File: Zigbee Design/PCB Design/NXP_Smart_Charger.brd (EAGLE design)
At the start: 108.3 x 63.3 mm, 83 parts, among them IC1 MID400, IC2 MID400, IC3 LMV358, IC4 LMV358, Q1 2222A, Q2 2222A

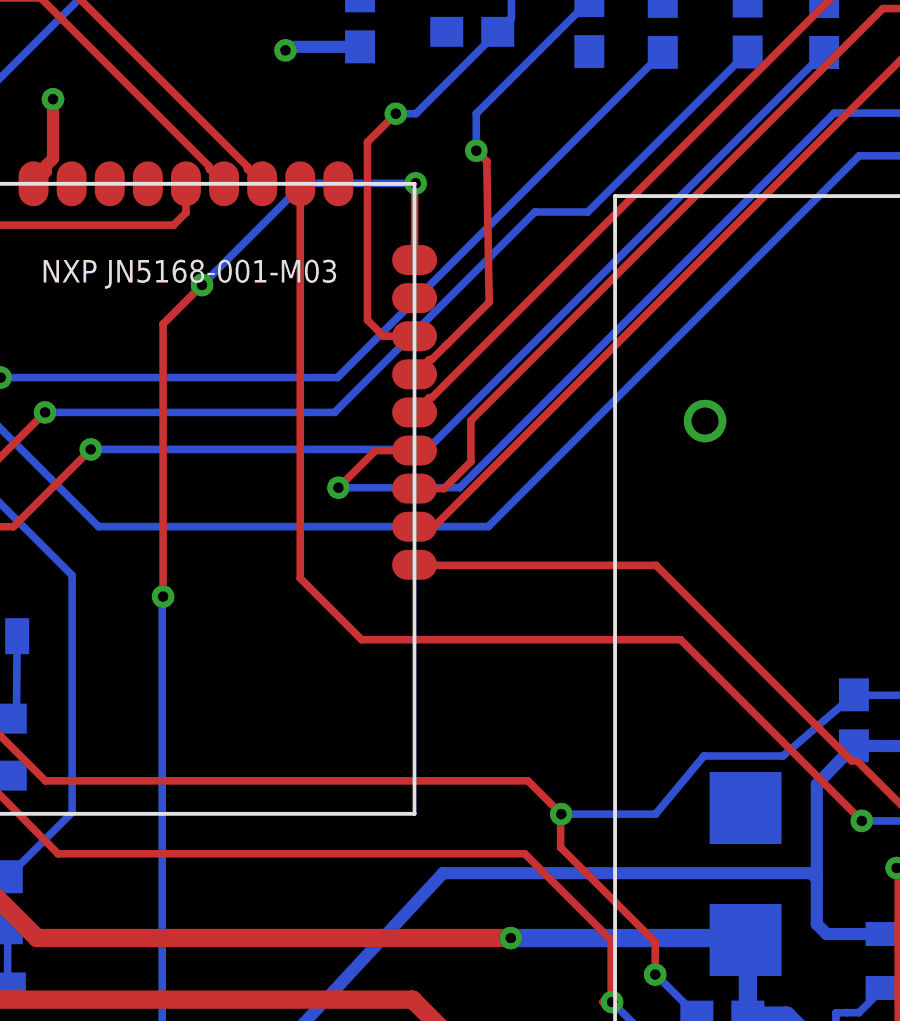
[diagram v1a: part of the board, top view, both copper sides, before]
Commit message: added flash memory
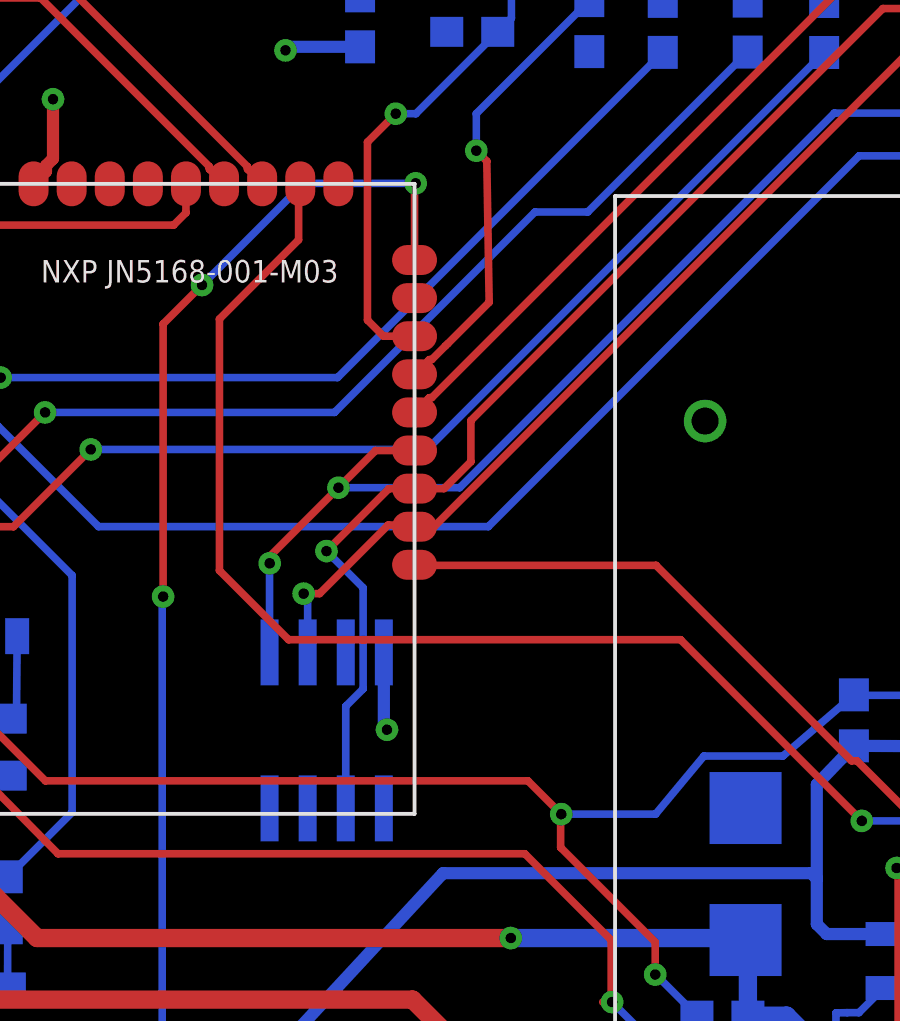
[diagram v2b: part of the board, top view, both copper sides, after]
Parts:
- added U1: M25P40, Smart_Charger:SO-08
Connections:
- new net HOLD: U1.7
- new net SS1: U1.1
- new net WP: U1.3
- net 3.3V: now also U1.8
- net GND: now also U1.4
- net MISO: now also U1.2
- net MOSI: now also U1.5
- net SPI_CLK: now also U1.6
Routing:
- net MISO: track 49.5 -> 62.7 mm, vias 0 -> 1
- net SPI_CLK: track 51.8 -> 58.5 mm, vias 0 -> 1
- net MOSI: track 59.4 -> 65.8 mm, vias 1 -> 2
- net PWM: track 45.6 -> 49.3 mm
- net 3.3V: track 32.0 -> 34.6 mm, vias 2 -> 3
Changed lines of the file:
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@@
 <attribute name="PROD_ID" value="CONN-08438" x="29.944059375" y="61.788040625" size="1.778" layer="27" display="off"/>
 </element>
+<element name="U1" library="Smart_Charger" package="SO-08" value="M25P40" x="31.407103125" y="33.853121875" rot="MR0"/>
 </elements>
 <signals>
@@
 <via x="49.24298125" y="30.8356" extent="1-16" drill="0.35"/>
 <wire x1="49.24298125" y1="30.8356" x2="43.2028625" y2="36.87571875" width="0.254" layer="1"/>
-<wire x1="43.2028625" y1="36.87571875" x2="32.572959375" y2="36.87571875" width="0.254" layer="1"/>
-<wire x1="32.572959375" y1="36.87571875" x2="30.52571875" y2="38.922959375" width="0.254" layer="1"/>
-<wire x1="30.52571875" y1="38.922959375" x2="30.52571875" y2="52.07254375" width="0.254" layer="1"/>
+<wire x1="43.2028625" y1="36.87571875" x2="32.654240625" y2="36.87571875" width="0.254" layer="1"/>
+<wire x1="32.654240625" y1="36.87571875" x2="32.572959375" y2="36.87571875" width="0.254" layer="1"/>
 <wire x1="54.188359375" y1="29.606240625" x2="52.959" y2="30.8356" width="0.254" layer="16"/>
+<wire x1="32.654240625" y1="36.87571875" x2="30.137103125" y2="36.87571875" width="0.254" layer="1"/>
+<wire x1="30.137103125" y1="36.87571875" x2="27.83078125" y2="39.182040625" width="0.254" layer="1"/>
+<wire x1="27.83078125" y1="39.182040625" x2="27.83078125" y2="47.564040625" width="0.254" layer="1"/>
+<wire x1="27.83078125" y1="47.564040625" x2="30.469840625" y2="50.2031" width="0.254" layer="1"/>
+<wire x1="30.469840625" y1="50.2031" x2="30.469840625" y2="52.016665625" width="0.254" layer="1"/>
+<wire x1="30.469840625" y1="52.016665625" x2="30.52571875" y2="52.07254375" width="0.254" layer="1"/>
 </signal>
 <signal name="N$2">
@@
 <wire x1="36.21278125" y1="44.1807625" x2="36.21278125" y2="42.809159375" width="0.254" layer="1"/>
 <wire x1="36.21278125" y1="42.809159375" x2="35.316165625" y2="41.91254375" width="0.254" layer="1"/>
-<wire x1="35.316165625" y1="41.91254375" x2="34.33571875" y2="41.91254375" width="0.254" layer="1"/>
+<wire x1="34.33571875" y1="41.91254375" x2="35.316165625" y2="41.91254375" width="0.254" layer="1"/>
+<contactref element="U1" pad="2"/>
+<wire x1="32.042103125" y1="31.253121875" x2="32.042103125" y2="34.657996875" width="0.254" layer="16"/>
+<wire x1="32.042103125" y1="34.657996875" x2="32.6215" y2="35.23739375" width="0.254" layer="16"/>
+<wire x1="32.6215" y1="35.23739375" x2="32.6215" y2="38.607721875" width="0.254" layer="16"/>
+<wire x1="32.6215" y1="38.607721875" x2="31.39948125" y2="39.829740625" width="0.254" layer="16"/>
+<via x="31.39948125" y="39.829740625" extent="1-16" drill="0.35"/>
+<wire x1="31.39948125" y1="39.829740625" x2="33.482284375" y2="41.91254375" width="0.254" layer="1"/>
+<wire x1="33.482284375" y1="41.91254375" x2="34.33571875" y2="41.91254375" width="0.254" layer="1"/>
 </signal>
 <signal name="MOSI">
@@
 <wire x1="31.798259375" y1="41.94301875" x2="33.037784375" y2="43.18254375" width="0.254" layer="1"/>
 <wire x1="33.037784375" y1="43.18254375" x2="34.33571875" y2="43.18254375" width="0.254" layer="1"/>
+<contactref element="U1" pad="5"/>
+<wire x1="29.502103125" y1="36.453121875" x2="29.502103125" y2="39.4182625" width="0.254" layer="16"/>
+<wire x1="29.502103125" y1="39.4182625" x2="29.50718125" y2="39.423340625" width="0.254" layer="16"/>
+<via x="29.50718125" y="39.423340625" extent="1-16" drill="0.35"/>
+<wire x1="29.50718125" y1="39.423340625" x2="29.50718125" y2="39.651940625" width="0.254" layer="1"/>
+<wire x1="29.50718125" y1="39.651940625" x2="31.798259375" y2="41.94301875" width="0.254" layer="1"/>
 </signal>
 <signal name="GND">
@@
 <wire x1="22.28341875" y1="52.91024375" x2="22.28341875" y2="54.891940625" width="0.4064" layer="1"/>
 <via x="22.28341875" y="54.891940625" extent="1-16" drill="0.35"/>
+<contactref element="U1" pad="4"/>
 </signal>
 <signal name="BUTTON3">
@@
 <wire x1="30.15175625" y1="56.638878125" x2="30.032959375" y2="56.52008125" width="0.4064" layer="16"/>
 <via x="30.032959375" y="56.52008125" extent="1-16" drill="0.35" shape="square"/>
+<contactref element="U1" pad="8"/>
+<wire x1="33.312103125" y1="36.453121875" x2="33.312103125" y2="33.98011875" width="0.4064" layer="16"/>
+<wire x1="33.312103125" y1="33.98011875" x2="33.416240625" y2="33.87598125" width="0.4064" layer="16"/>
+<via x="33.416240625" y="33.87598125" extent="1-16" drill="0.35"/>
 </signal>
 <signal name="N$5">
@@
 <wire x1="75.4334" y1="56.45911875" x2="50.8" y2="56.45911875" width="0.254" layer="1"/>
 <wire x1="50.8" y1="56.45911875" x2="34.983425" y2="40.64254375" width="0.254" layer="1"/>
-<wire x1="34.983425" y1="40.64254375" x2="34.33571875" y2="40.64254375" width="0.254" layer="1"/>
+<wire x1="34.33571875" y1="40.64254375" x2="34.983425" y2="40.64254375" width="0.254" layer="1"/>
+<contactref element="U1" pad="6"/>
+<wire x1="30.772103125" y1="36.453121875" x2="30.772103125" y2="38.277796875" width="0.254" layer="16"/>
+<wire x1="30.772103125" y1="38.277796875" x2="30.63748125" y2="38.41241875" width="0.254" layer="16"/>
+<via x="30.63748125" y="38.41241875" extent="1-16" drill="0.35"/>
+<wire x1="30.63748125" y1="38.41241875" x2="31.17088125" y2="38.41241875" width="0.254" layer="1"/>
+<wire x1="31.17088125" y1="38.41241875" x2="33.45688125" y2="40.69841875" width="0.254" layer="1"/>
+<wire x1="33.45688125" y1="40.69841875" x2="34.27984375" y2="40.69841875" width="0.254" layer="1"/>
+<wire x1="34.27984375" y1="40.69841875" x2="34.33571875" y2="40.64254375" width="0.254" layer="1"/>
 </signal>
 <signal name="L6">
@@
 <wire x1="33.3019375" y1="46.99254375" x2="34.33571875" y2="46.99254375" width="0.254" layer="1"/>
 </signal>
+<signal name="HOLD">
+<contactref element="U1" pad="7"/>
+</signal>
+<signal name="SS1">
+<contactref element="U1" pad="1"/>
+</signal>
+<signal name="WP">
+<contactref element="U1" pad="3"/>
+</signal>
 </signals>

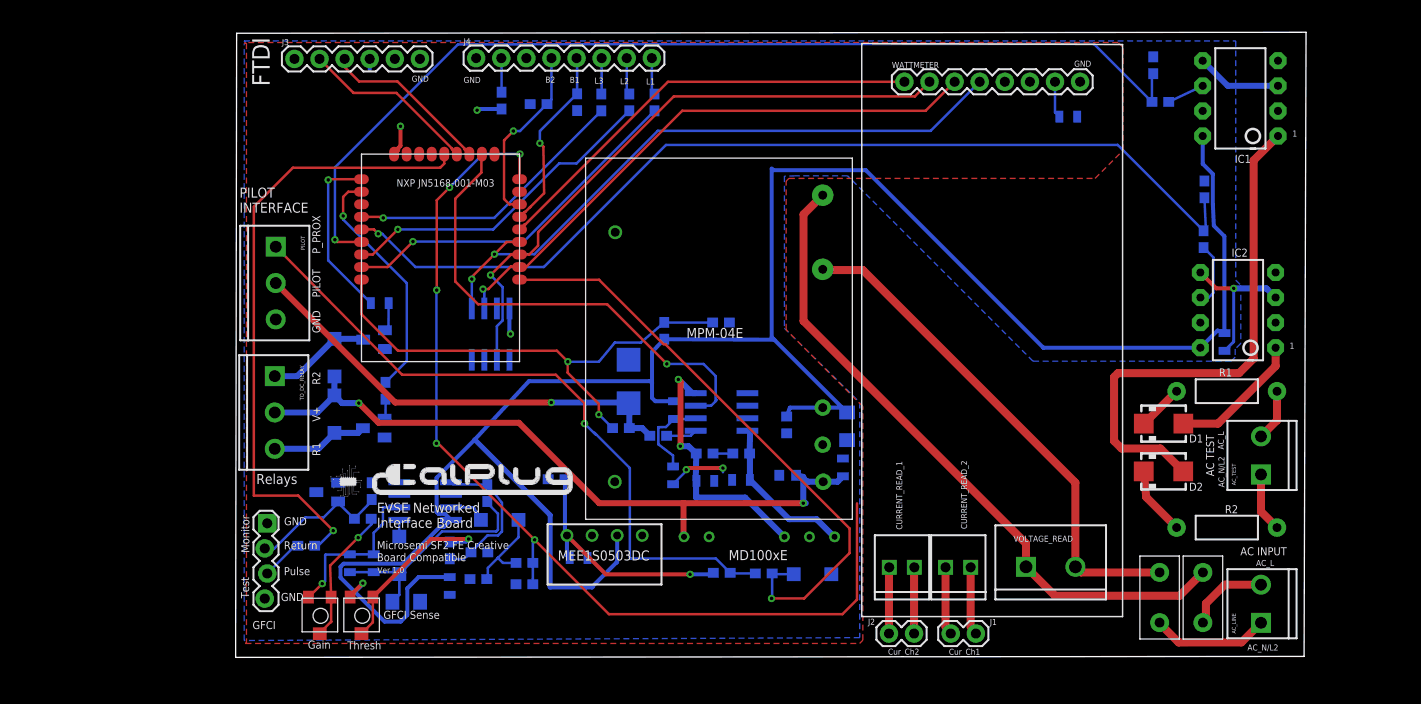
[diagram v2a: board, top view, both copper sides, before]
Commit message: added smartenit eagle file
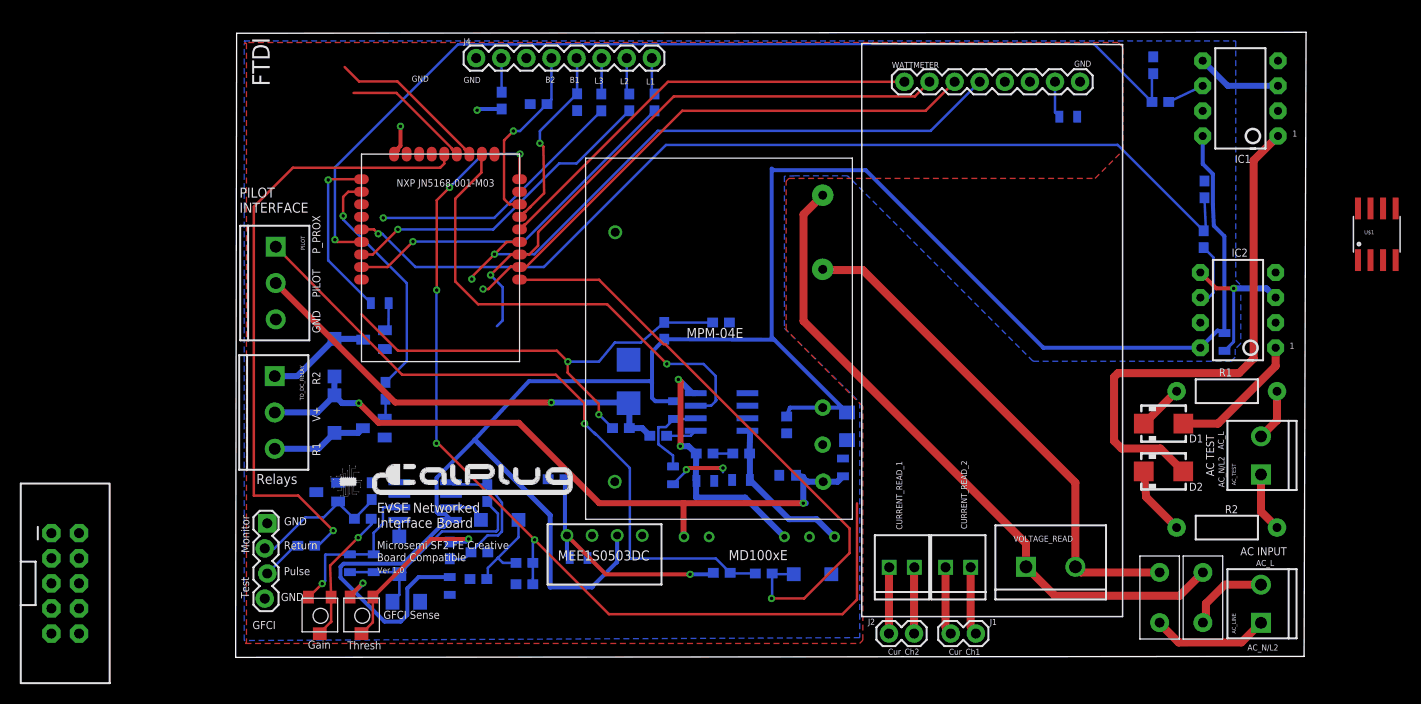
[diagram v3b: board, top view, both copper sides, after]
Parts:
- removed J3: (no value), SparkFun-Connectors:1X06
- removed U1: M25P40, Smart_Charger:SO-08
- added U$1: SPI_FLASH-X25XXSMD, SparkFun:SO08
- added U$2: AVR_SPI_PROG2LOCK, SparkFun:2X5-SHROUDED_LOCK
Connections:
- removed net BUTTON3: JN5168.P8
- removed net HOLD: U1.7
- removed net L4: JN5168.P21
- removed net L5: JN5168.P16
- removed net L6: JN5168.P15
- removed net L9: JN5168.P10
- removed net WP: U1.3
- new net RESET: JN5168.P22
- net 3.3V: now also JN5168.P27, U$1.3; no longer J3.4, U1.8
- net GND: now also U$1.4; no longer J3.6, U1.4
- net L3: now also JN5168.P21; no longer JN5168.P22
- net MISO: now also U$1.2; no longer U1.2
- net MOSI: no longer U1.5
- net PILOTREAD: now also JN5168.P8; no longer JN5168.P27
- net RX: no longer J3.2
- net SPI_CLK: no longer U1.6
- net SS1: now also JN5168.P10, U$1.1; no longer U1.1
- net TX: no longer J3.3
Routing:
- net RX: track 18.1 -> 13.1 mm
- net 3.3V: track 34.6 -> 30.9 mm, vias 3 -> 2
- net PILOTREAD: track 51.4 -> 47.9 mm
- net MISO: track 62.7 -> 59.3 mm
- net MOSI: track 65.8 -> 62.9 mm
- net L3: track 28.8 -> 26.7 mm
- net SPI_CLK: track 58.5 -> 56.7 mm
- net TX: track 17.1 -> 16.3 mm
